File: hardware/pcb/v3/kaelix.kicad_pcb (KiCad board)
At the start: 2 copper layers, 61 x 51 mm, 44 parts, among them J1 LiPo 3,7V, J2 UART/BOOT, J3 USB-C 5V, Q1 SI2301CDS, Q2 BC847B, Q3 SI2301CDS, U1 ESP32-S3-WROOM-1U-N16R8, U2 MPU-6050, U3 Ai-Thinker Ra-02 (SX1278), U4 HT7333, U5 BQ21040DBV

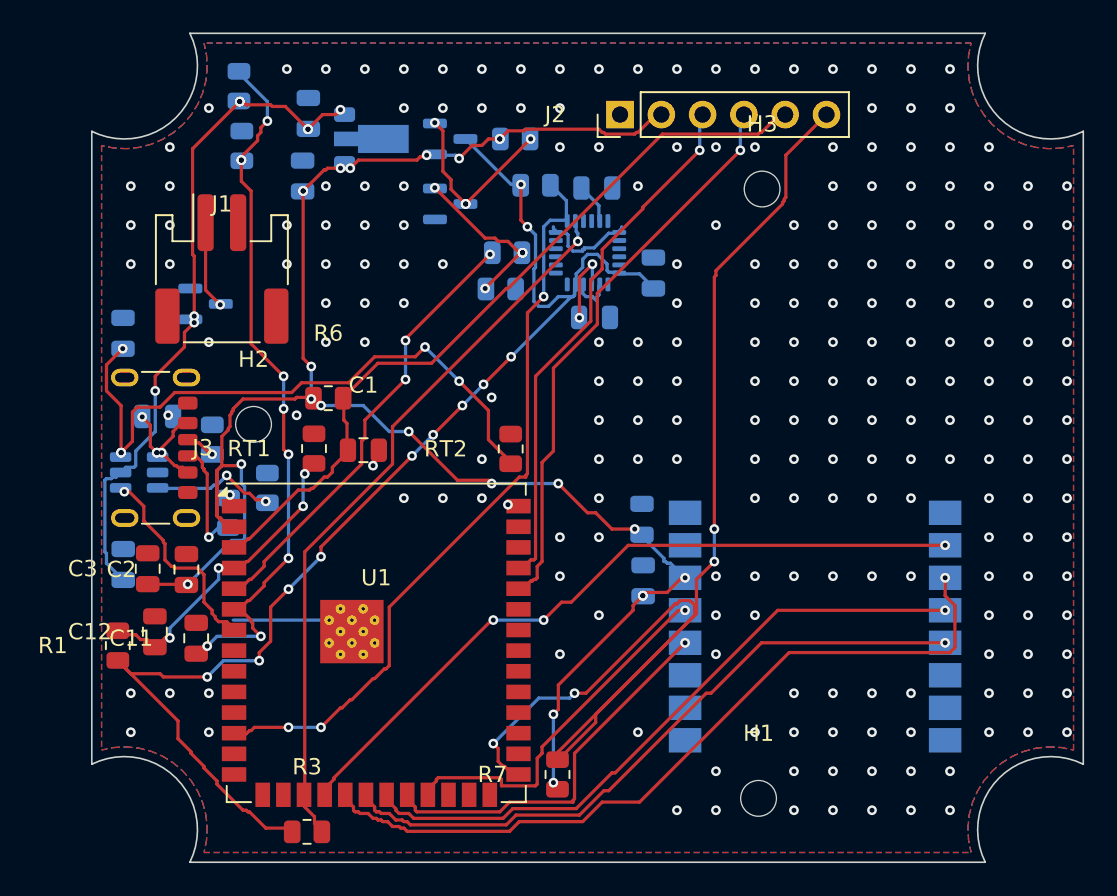
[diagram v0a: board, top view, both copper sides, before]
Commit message: Add BOM, designators, and positions CSV files; update build script for drill hole checks
- Created bom.csv to list components with designators, footprints, quantities, values, and LCSC part numbers.
- Added designators.csv to map designators to their respective counts.
- Introduced positions.csv to specify the midpoints, rotation, and layer for each component.
- Updated build-hardware.sh to include checks for overlapping drill holes, ensuring compliance with manufacturing guidelines.
- Modified render_bottom.png and render_top.png to reflect the latest design changes.
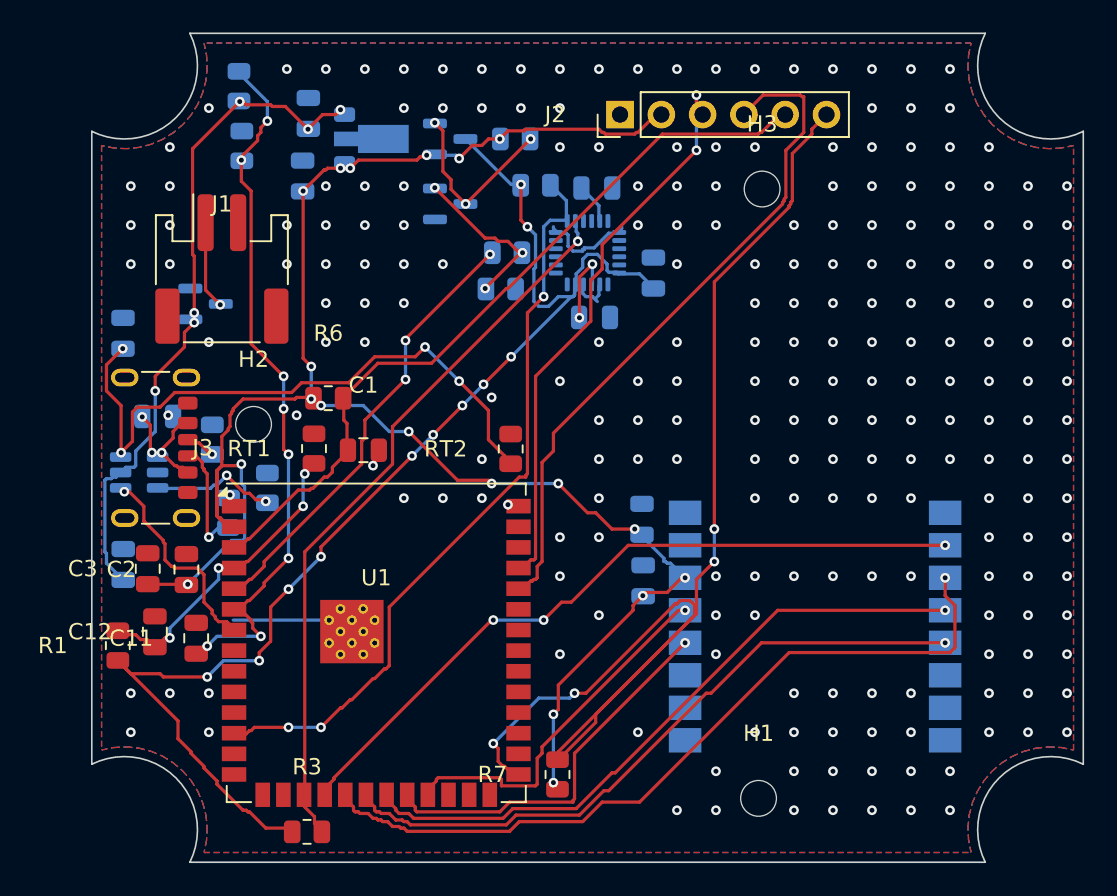
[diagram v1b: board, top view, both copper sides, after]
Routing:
- net UART_RX: track 35.3 -> 42.1 mm, vias 2 -> 0
- net UART_TX: track 32.9 -> 35.3 mm
- net VBUS: vias 4 -> 3
- net VBAT_SENSE: vias 9 -> 8
- net VBAT: vias 8 -> 6
- net PERIPH_GATE: vias 4 -> 3
- net PERIPH_BASE: vias 4 -> 3
- net GND: vias 226 -> 228
- net CHG_TS: vias 5 -> 4
- net +3V3: vias 22 -> 19
